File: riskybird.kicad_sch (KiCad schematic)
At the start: 23 parts, among them U1 MCP73831-2-OT, U2 MPU-9150, U3 TPS2113A, U4 ESP32-S3-WROOM-2, U5 MPL3115A2

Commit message: update schematic with USB-UART, IMU, and Power
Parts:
- removed U4: ESP32-S3-WROOM-2, Espressif:ESP32-S3-WROOM-2, symbol Espressif:ESP32-S3-WROOM-2
- added C10, C12: 4.7u, Capacitor_SMD:C_0805_2012Metric_Pad1.15x1.40mm_HandSolder, symbol Device:C
- added C11: 10n, Capacitor_SMD:C_0805_2012Metric_Pad1.15x1.40mm_HandSolder, symbol Device:C
- added C13: 0.1u, Capacitor_SMD:C_0805_2012Metric_Pad1.15x1.40mm_HandSolder, symbol Device:C
- added D2, D3, D4, D5: BAT54JFILM, Diode_SMD:D_SOD-323_HandSoldering, symbol Diode:BAT54J
- added FID1: DroneFrame, riskybird:riskybird_frame, symbol Mechanical:Fiducial
- added J1: USB_B_Micro, Connector_USB:USB_Micro-B_Molex_47346-0001, symbol Connector:USB_B_Micro
- added J2, J3, J4, J5: Conn_01x02, Connector_Molex:Molex_PicoBlade_53048-0210_1x02_P1.25mm_Horizontal, symbol Connector_Generic:Conn_01x02
- added J6: Conn_01x02, symbol Connector_Generic:Conn_01x02
- added JP6, JP7: SolderJumper_2_Bridged, Jumper:SolderJumper-2_P1.3mm_Bridged_Pad1.0x1.5mm, symbol Jumper:SolderJumper_2_Bridged
- added L1: 1uH, symbol Device:L
- added Q1, Q2, Q3, Q4: Q_NMOS_GSD, symbol Device:Q_NMOS_GSD
- added Q5, Q6: DNBT8105-7, Package_TO_SOT_SMD:SOT-23_Handsoldering, symbol Device:Q_NPN_BEC
- added R10, R13, R15, R17, R20, R21, R4, R5, R6, R7: 10k, Resistor_SMD:R_0805_2012Metric_Pad1.20x1.40mm_HandSolder, symbol Device:R
- added R11, R12, R14, R16: 47R, Resistor_SMD:R_0805_2012Metric_Pad1.20x1.40mm_HandSolder, symbol Device:R
- added R18, R19: 27, Resistor_SMD:R_0805_2012Metric_Pad1.20x1.40mm_HandSolder, symbol Device:R
- added R8, R9: 2.2k, Resistor_SMD:R_0805_2012Metric_Pad1.20x1.40mm_HandSolder, symbol Device:R
- added U4: LP2985-3.0, Package_TO_SOT_SMD:SOT-23-5, symbol Regulator_Linear:LP2985-3.0
- added U6: ESP32-C3-WROOM-02, Espressif:ESP32-C3-WROOM-02, symbol Espressif:ESP32-C3-WROOM-02
- added U8: FT231XS, Package_SO:SSOP-20_3.9x8.7mm_P0.635mm, symbol Interface_USB:FT231XS
- C1, C2, C4, C7, C8, C9: footprint (none) -> Capacitor_SMD:C_0805_2012Metric_Pad1.15x1.40mm_HandSolder
- R2, R3: footprint (none) -> Resistor_SMD:R_0805_2012Metric_Pad1.20x1.40mm_HandSolder
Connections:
- net GNDA is gone; now on net GND: C3.2, C4.2, C5.2, C6.2, C7.2, C8.2, C9.2, JP1.1 (A), JP2.2 (B), JP3.2 (B), U2.15 (GND), U2.17 (GND), U2.18 (GND), U5.3 (GND)
- net VUSB is gone; now on net +5V: C1.1, R2.1, U1.4 (VDD)
- net GND: now also C1.2, R1.2, U1.2 (VSS), C10.2, C11.2, C12.2, C13.2, J1.5 (GND), J1.6 (Shield), J6.2 (Pin_2), Q1.2 (S), Q2.2 (S), Q3.2 (S), Q4.2 (S), R10.2, R13.2, R15.2, R17.2, R5.2, R7.2, U4.2 (GND), U6.19 (GND), U6.9 (GND), U8.16 (GND), U8.6 (GND)
- net SCL: now also R9.2, U6.6 (GPIO7)
- net SDA: now also R8.2, U6.5 (GPIO6)
- net VBAT: no longer C2.1, U3.6 (IN2)
- net VCOM: now also U4.1 (VIN)
- net VDDA: now also C12.1, L1.2
- net at U3.1 (STAT): now also R7.1
- net at U3.3 (VSNS): now also R6.2
- net +5V: now reaches U3.8 (IN1)
- net +5V: now also J1.1 (VBUS), R4.1, R6.1, U8.15 (VCC)
- new net: Q1.1 (G), R12.2, R13.1
- new net: D3.2 (A), J3.2 (Pin_2), Q1.3 (D)
- new net: C11.1, U4.4 (BP)
- new net: D5.2 (A), J5.2 (Pin_2), Q4.3 (D)
- new net: Q5.1 (B), R20.2
- new net: D4.2 (A), J4.2 (Pin_2), Q3.3 (D)
- new net: Q4.1 (G), R16.2, R17.1
- new net: Q2.1 (G), R10.1, R11.2
- new net: D2.2 (A), J2.2 (Pin_2), Q2.3 (D)
- new net: JP7.1 (A), U8.4 (RXD)
- new net: Q3.1 (G), R14.2, R15.1
- new net: R19.2, U8.11 (USBDP)
- new net: R18.2, U8.12 (USBDM)
- new net: JP6.1 (A), U8.20 (TXD)
- new net: Q6.1 (B), R21.2
- new net +BATT: C2.1, D2.1 (K), D3.1 (K), D4.1 (K), D5.1 (K), J2.1 (Pin_1), J3.1 (Pin_1), J4.1 (Pin_1), J5.1 (Pin_1), J6.1 (Pin_1), U3.6 (IN2)
- new net CHIP_EN: Q5.3 (C), U6.2 (EN/CHIP_PU)
- new net DTR: Q6.2 (E), R20.1, U8.1 (~{DTR})
- new net GPIO9: Q6.3 (C), U6.8 (GPIO9)
- new net MOTOR1: R11.1
- new net MOTOR2: R12.1
- new net MOTOR3: R14.1
- new net MOTOR4: R16.1
- new net RTS: Q5.2 (E), R21.1, U8.2 (~{RTS})
- new net U0RXD: U6.11 (GPIO20/U0RXD)
- new net U0TXD: JP7.2 (B), U6.12 (GPIO21/U0TXD)
- new net UORXD: JP6.2 (B)
- new net USB_DM: J1.2 (D-), R18.1
- new net USB_DP: J1.3 (D+), R19.1
- new net VDD: C10.1, C13.1, L1.1, R8.1, R9.1, U4.5 (VOUT), U6.1 (3V3), U8.14 (~{RESET}), U8.3 (VCCIO)
- new net VEN_D: R4.2, R5.1, U4.3 (ON/~{OFF})
- no-connect marks 2 -> 12
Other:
- added sheet Power (riskybird_power.kicad_sch)
- moved on the sheet: C1, C2, D1, R1, R2, R3, U1, U3

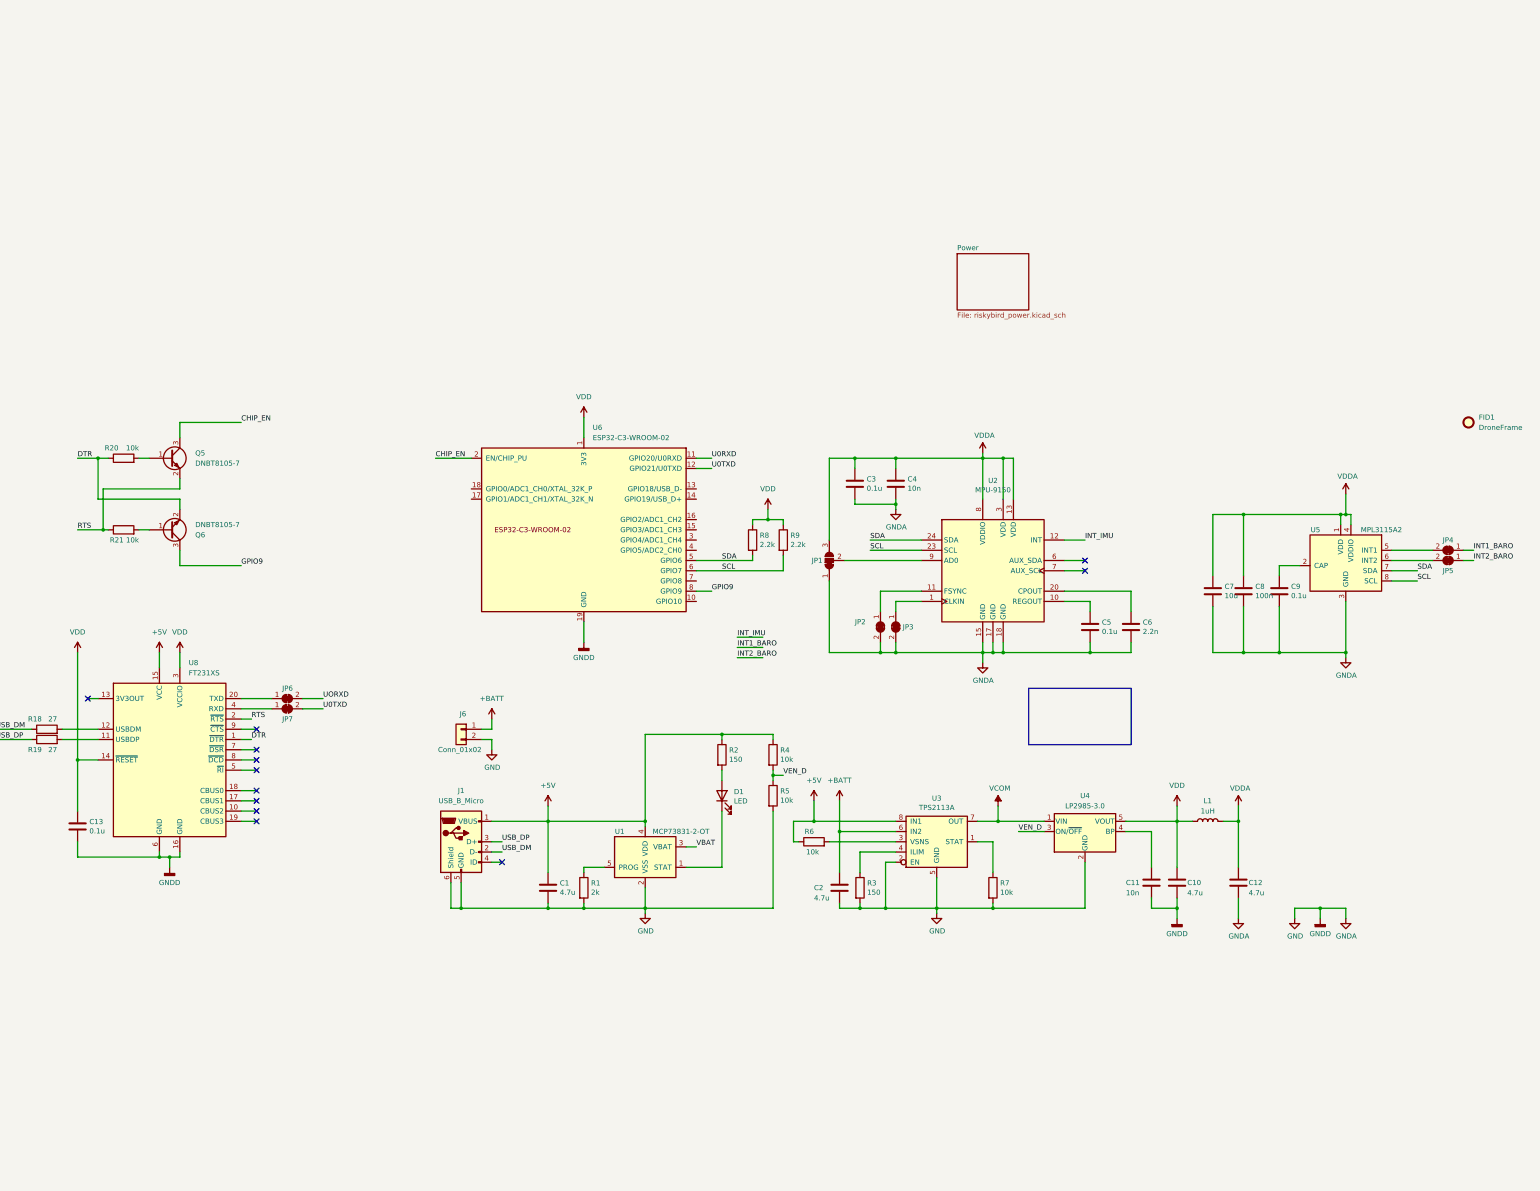
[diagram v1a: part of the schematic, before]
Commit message: add baro footprint, switches, make passives 0603
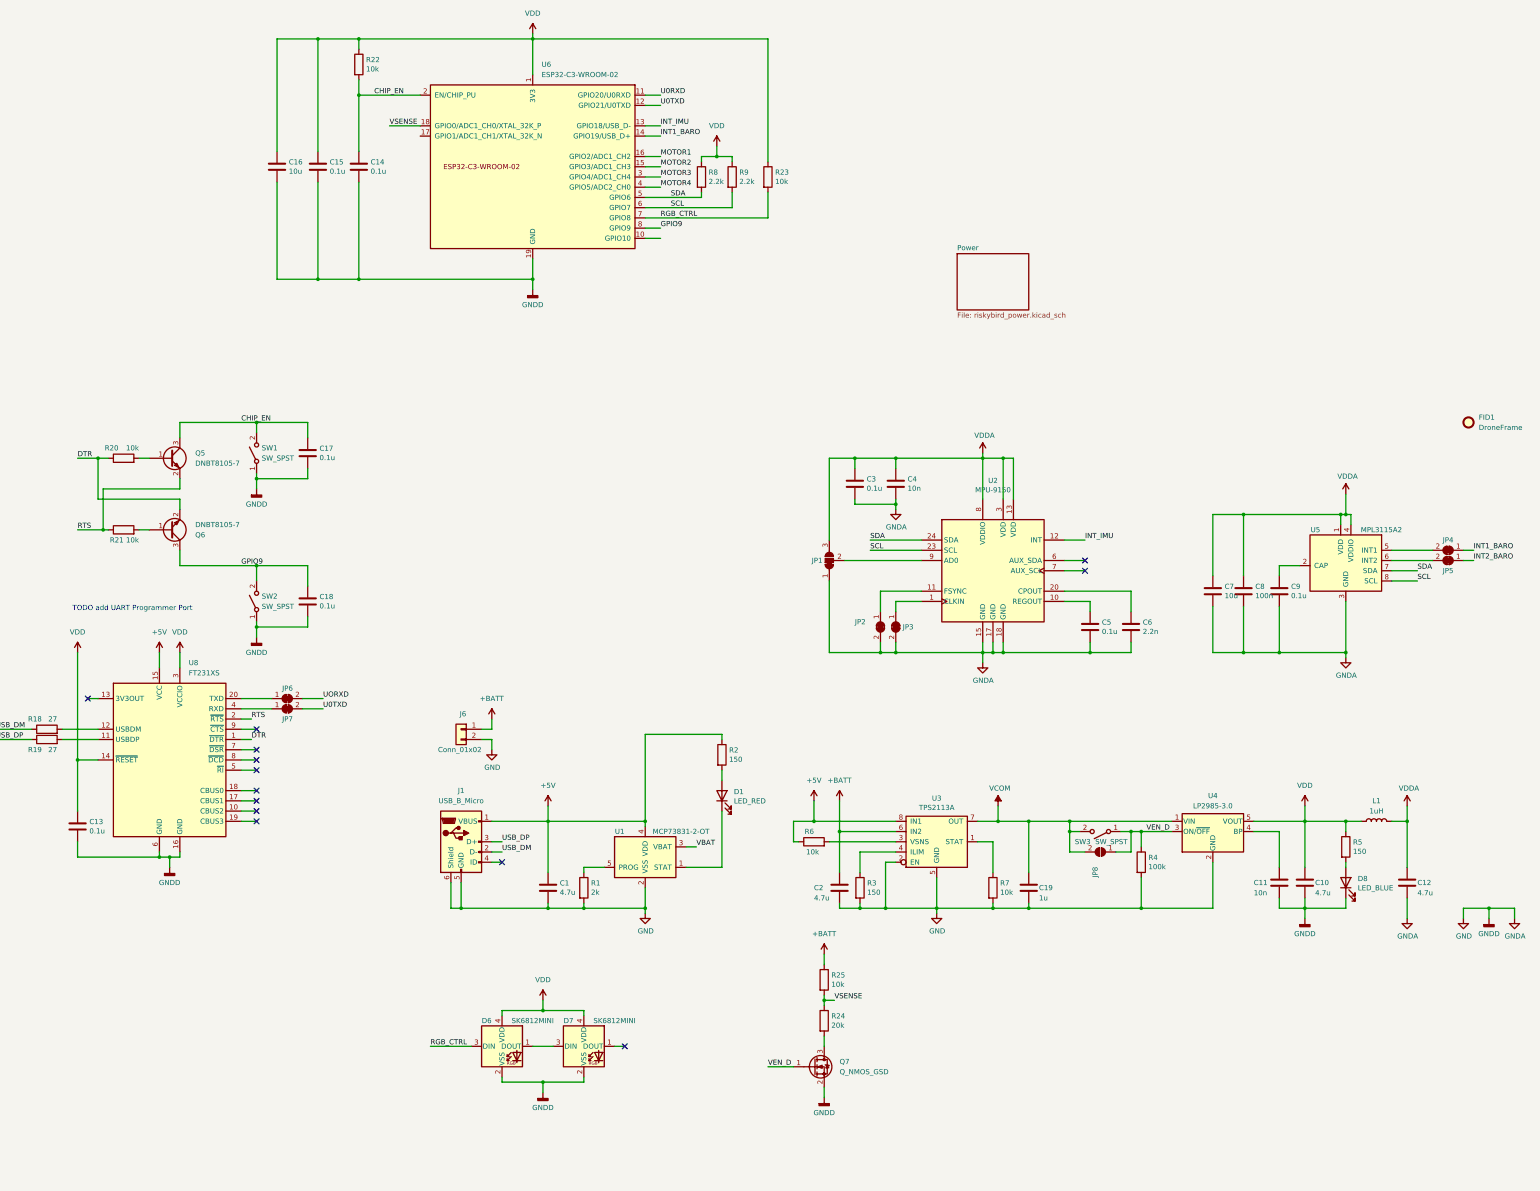
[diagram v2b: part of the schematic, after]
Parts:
- added C14, C15, C17, C18: 0.1u, Capacitor_SMD:C_0603_1608Metric_Pad1.08x0.95mm_HandSolder, symbol Device:C
- added C16: 10u, Capacitor_SMD:C_0603_1608Metric_Pad1.08x0.95mm_HandSolder, symbol Device:C
- added C19: 1u, Capacitor_SMD:C_0603_1608Metric_Pad1.08x0.95mm_HandSolder, symbol Device:C
- added D6, D7: SK6812MINI, LED_SMD:LED_SK6812MINI_PLCC4_3.5x3.5mm_P1.75mm, symbol LED:SK6812MINI
- added D8: LED_BLUE, LED_SMD:LED_0805_2012Metric_Pad1.15x1.40mm_HandSolder, symbol Device:LED
- added JP8: SolderJumper_2_Open, Jumper:SolderJumper-2_P1.3mm_Open_Pad1.0x1.5mm, symbol Jumper:SolderJumper_2_Open
- added Q7: Q_NMOS_GSD, symbol Device:Q_NMOS_GSD
- added R22, R25: 10k, Resistor_SMD:R_0603_1608Metric_Pad0.98x0.95mm_HandSolder, symbol Device:R
- added R23: 10k, Resistor_SMD:R_0805_2012Metric_Pad1.20x1.40mm_HandSolder, symbol Device:R
- added R24: 20k, Resistor_SMD:R_0603_1608Metric_Pad0.98x0.95mm_HandSolder, symbol Device:R
- added SW1, SW2: SW_SPST, Button_Switch_SMD:SW_SPST_B3U-1000P, symbol Switch:SW_SPST
- added SW3: SW_SPST, Button_Switch_SMD:SW_SPDT_CK-JS102011SAQN, symbol Switch:SW_SPST
- C1, C10, C11, C12, C13, C2, C3, C4, C5, C6, C7, C8, C9: footprint Capacitor_SMD:C_0805_2012Metric_Pad1.15x1.40mm_HandSolder -> Capacitor_SMD:C_0603_1608Metric_Pad1.08x0.95mm_HandSolder
- D1: value LED -> LED_RED; footprint (none) -> LED_SMD:LED_0805_2012Metric_Pad1.15x1.40mm_HandSolder
- R1: footprint (none) -> Resistor_SMD:R_0603_1608Metric_Pad0.98x0.95mm_HandSolder
- R10, R11, R12, R13, R14, R15, R16, R17, R18, R19, R2, R20, R21, R3, R6, R7: footprint Resistor_SMD:R_0805_2012Metric_Pad1.20x1.40mm_HandSolder -> Resistor_SMD:R_0603_1608Metric_Pad0.98x0.95mm_HandSolder
- R4: value 10k -> 100k; footprint Resistor_SMD:R_0805_2012Metric_Pad1.20x1.40mm_HandSolder -> Resistor_SMD:R_0603_1608Metric_Pad0.98x0.95mm_HandSolder
- R5: value 10k -> 150; footprint Resistor_SMD:R_0805_2012Metric_Pad1.20x1.40mm_HandSolder -> Resistor_SMD:R_0603_1608Metric_Pad0.98x0.95mm_HandSolder
- U5: footprint (none) -> riskybird:MPL3115A2
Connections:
- net +5V: no longer R4.1
- net +BATT: now also R25.1
- net CHIP_EN: now also C14.1, C17.1, R22.2, SW1.2 (B)
- net GND: now also R4.2, C14.2, C15.2, C16.2, C17.2, C18.2, C19.2, D6.2 (VSS), D7.2 (VSS), D8.1 (K), Q7.2 (S), SW1.1 (A), SW2.1 (A); no longer R5.2
- net GPIO9: now also C18.1, SW2.2 (B)
- net INT1_BARO: now also U6.14 (GPIO19/USB_D+)
- net INT_IMU: now also U6.13 (GPIO18/USB_D-)
- net MOTOR1: now also U6.16 (GPIO2/ADC1_CH2)
- net MOTOR2: now also U6.15 (GPIO3/ADC1_CH3)
- net MOTOR3: now also U6.3 (GPIO4/ADC1_CH4)
- net MOTOR4: now also U6.4 (GPIO5/ADC2_CH0)
- net VCOM: now also C19.1, JP8.2 (B), SW3.2 (B)
- net VDD: now also R5.1, C15.1, C16.1, D6.4 (VDD), D7.4 (VDD), R22.1, R23.1
- net VEN_D: now also R4.1, JP8.1 (A), Q7.1 (G), SW3.1 (A); no longer R4.2, R5.1
- net VSENSE: now reaches U6.18 (GPIO0/ADC1_CH0/XTAL_32K_P)
- net VSENSE: now also R24.1, R25.2
- net RGB_CTRL: now reaches U6.7 (GPIO8)
- net RGB_CTRL: now also D6.3 (DIN), R23.2
- new net: D6.1 (DOUT), D7.3 (DIN)
- new net: Q7.3 (D), R24.2
- new net: D8.2 (A), R5.2
- no-connect marks 12 -> 13
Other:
- note added: "TODO add UART Programmer Port"
- moved on the sheet: C10, C11, C12, L1, R8, R9, U4, U6
